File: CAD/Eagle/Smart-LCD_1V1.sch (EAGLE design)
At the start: 49 parts, among them Q121 MMBT2222AL, U101 MEGA8-P, U221 MCP4018T-104E/LT, U401 TS4871ID, X131 LDR, X141 Switches, X151 LEDs, X201 LCD_23WAY__UC1608, X231 LED_A, X232 LED_K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

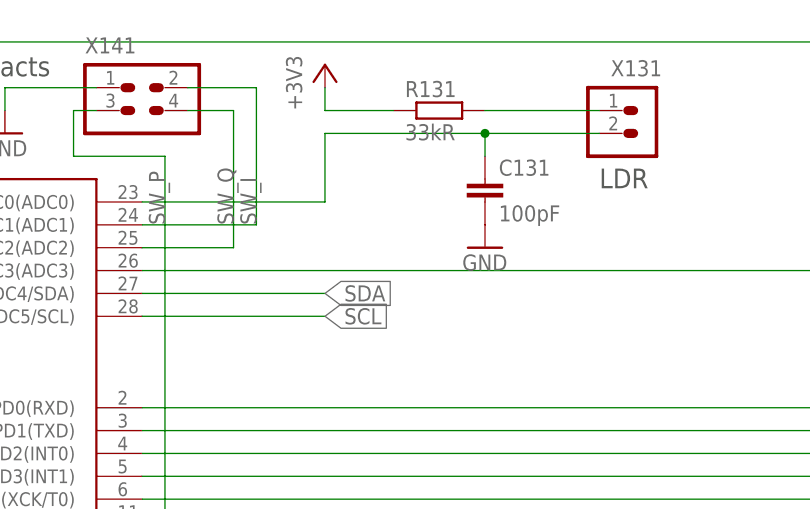
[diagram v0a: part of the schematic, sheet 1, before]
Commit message: CAD - new version V1.1 - missing resistor for LDR added, missing header pin number 1 marking added
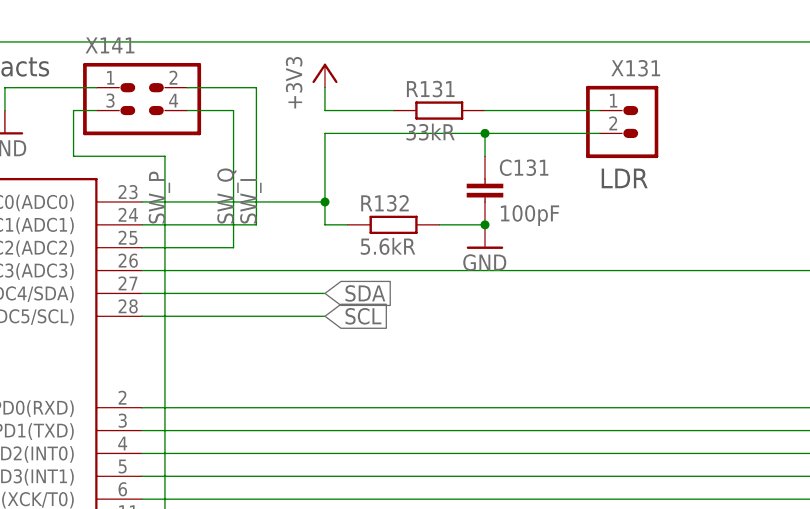
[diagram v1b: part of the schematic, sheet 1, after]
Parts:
- added R132: 5.6kR, rcl:R-EU_R0805
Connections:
- net GND: now also R132.2
- net LDR: now also R132.1
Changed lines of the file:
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@@
 <part name="C455" library="rcl" deviceset="C-EU" device="C0805" value="470nF"/>
 <part name="C452" library="rcl" deviceset="C-EU" device="C0805" value="470pF"/>
+<part name="R132" library="rcl" deviceset="R-EU_" device="R0805" value="5.6kR"/>
 </parts>
 <sheets>
@@
 <instance part="GND111" gate="1" x="154.94" y="53.34"/>
 <instance part="X141" gate="G$1" x="134.62" y="152.4"/>
+<instance part="R132" gate="G$1" x="162.56" y="137.16"/>
 </instances>
 <busses>
@@
 <pinref part="C131" gate="G$1" pin="2"/>
 <pinref part="GND131" gate="1" pin="GND"/>
+<pinref part="R132" gate="G$1" pin="2"/>
+<wire x1="172.72" y1="137.16" x2="167.64" y2="137.16" width="0.1524" layer="91"/>
+<junction x="172.72" y="137.16"/>
 </segment>
 <segment>
@@
 <pinref part="X131" gate="A" pin="2"/>
 <pinref part="U101" gate="G$1" pin="PC0(ADC0)"/>
-</segment>
-</net>
+<wire x1="154.94" y1="139.7" x2="154.94" y2="137.16" width="0.1524" layer="91"/>
+<pinref part="R132" gate="G$1" pin="1"/>
+<wire x1="154.94" y1="137.16" x2="157.48" y2="137.16" width="0.1524" layer="91"/>
+<junction x="154.94" y="139.7"/>
+</segment>
+</net>

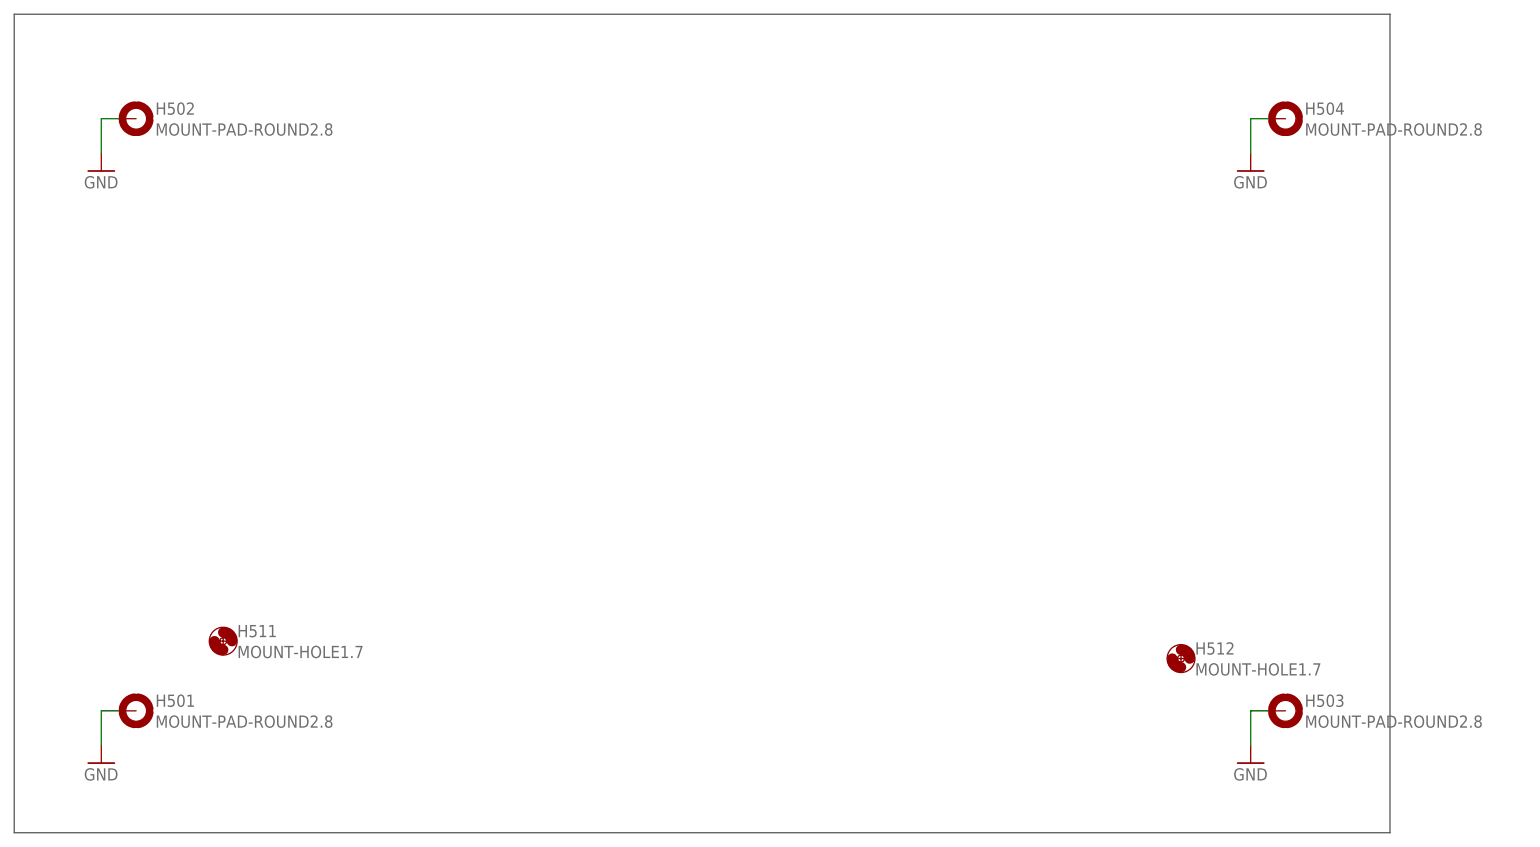
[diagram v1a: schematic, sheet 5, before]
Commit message: CAD - four fiducials added
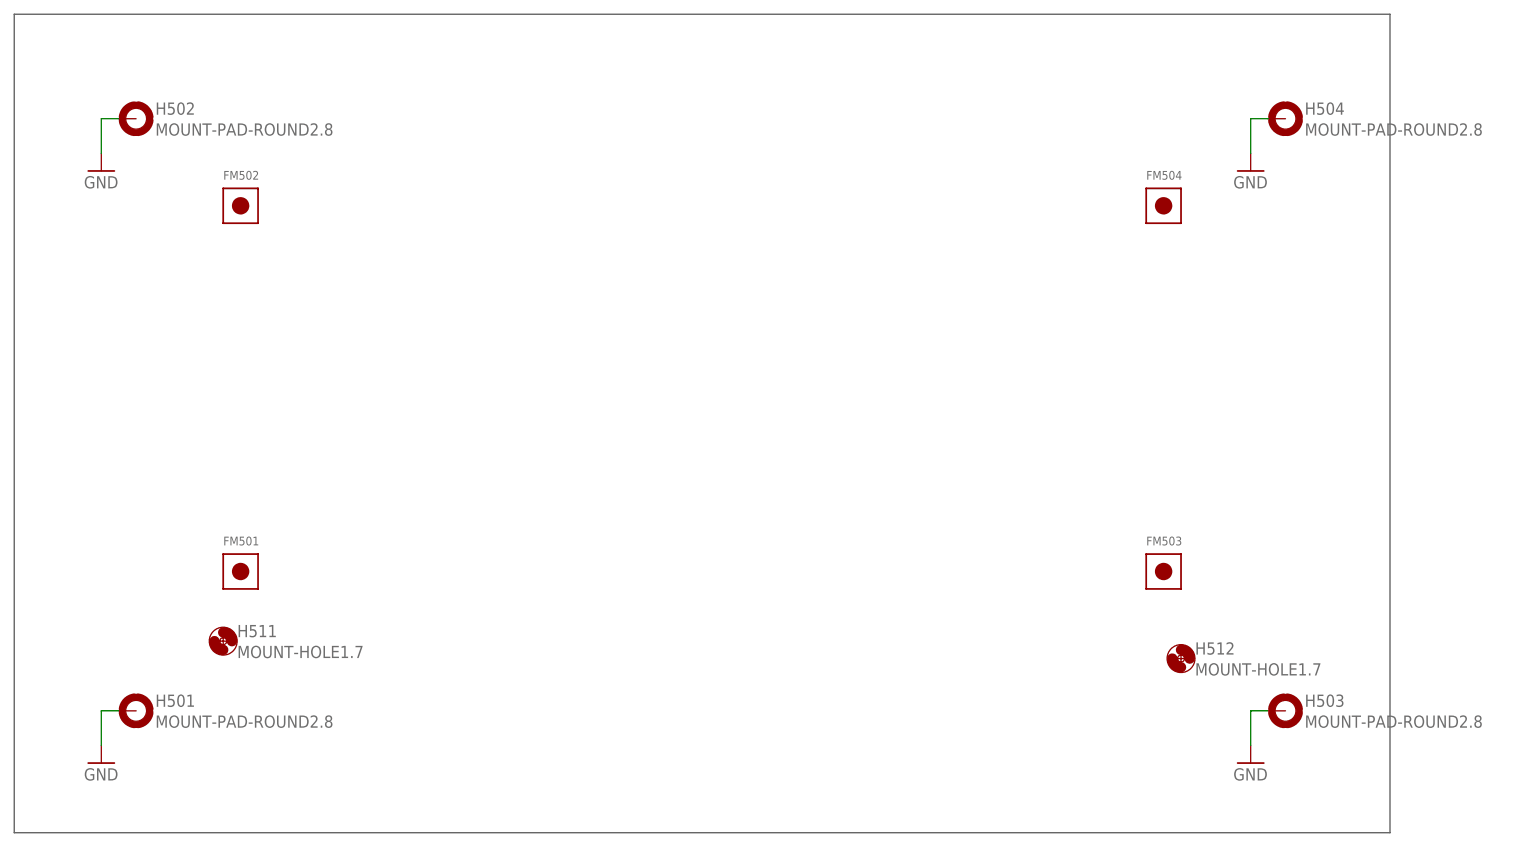
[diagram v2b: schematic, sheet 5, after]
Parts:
- added FM501, FM502, FM503, FM504: FIDUCIAL_MARK_1MM, df4iah_fiducial:FIDUCIAL_MARK_1MM
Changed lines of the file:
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@@
 <part name="C452" library="rcl" deviceset="C-EU" device="C0805" value="470pF"/>
 <part name="R132" library="rcl" deviceset="R-EU_" device="R0805" value="5.6kR"/>
+<part name="FM502" library="df4iah_fiducial" deviceset="FIDUCIAL_MARK_1MM" device=""/>
+<part name="FM501" library="df4iah_fiducial" deviceset="FIDUCIAL_MARK_1MM" device=""/>
+<part name="FM503" library="df4iah_fiducial" deviceset="FIDUCIAL_MARK_1MM" device=""/>
+<part name="FM504" library="df4iah_fiducial" deviceset="FIDUCIAL_MARK_1MM" device=""/>
 </parts>
 <sheets>
@@
 <instance part="H511" gate="G$1" x="55.88" y="68.58"/>
 <instance part="H512" gate="G$1" x="195.58" y="66.04"/>
+<instance part="FM502" gate="G$1" x="58.42" y="132.08"/>
+<instance part="FM501" gate="G$1" x="58.42" y="78.74"/>
+<instance part="FM503" gate="G$1" x="193.04" y="78.74"/>
+<instance part="FM504" gate="G$1" x="193.04" y="132.08"/>
 </instances>
 <busses>

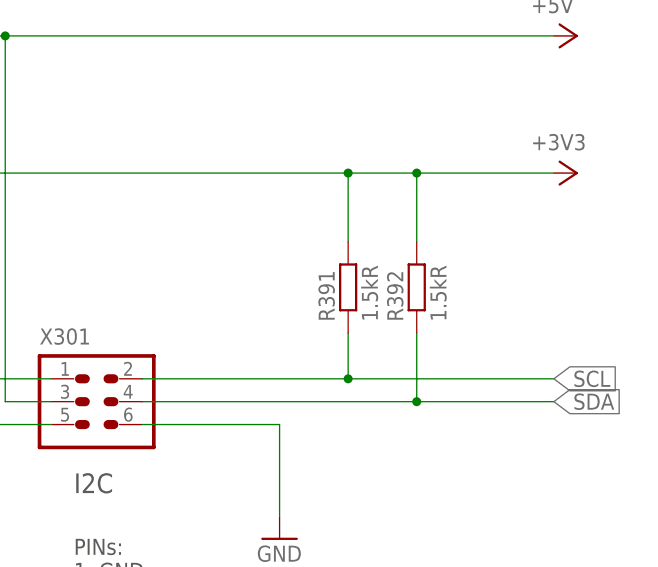
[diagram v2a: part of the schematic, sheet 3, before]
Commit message: HW_V1.1 - LCD backlight basis resistor chnaged to 4.7k ohms
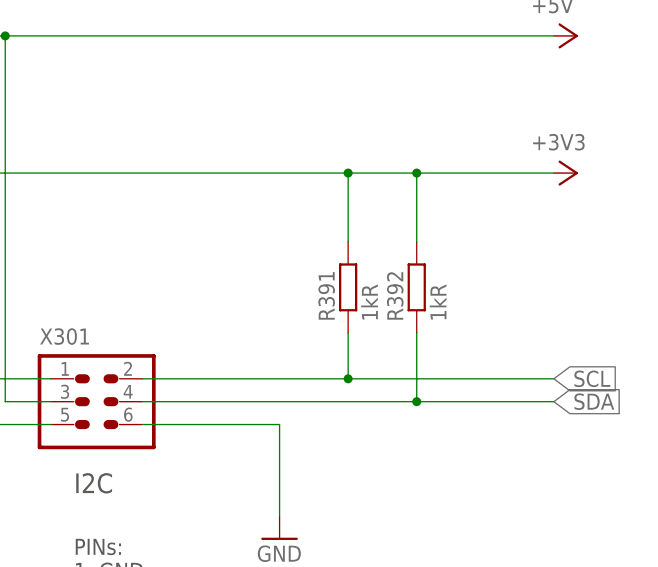
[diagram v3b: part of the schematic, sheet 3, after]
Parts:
- R121: value 18kR -> 4.7kR
- R391, R392: value 1.5kR -> 1kR; device rcl:R-EU_R0603 -> rcl:R-EU_R0805
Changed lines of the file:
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@@
 <part name="+3V3_301" library="df4iah_supply" deviceset="+3V3" device=""/>
 <part name="+5V0_301" library="df4iah_supply" deviceset="+5V" device=""/>
-<part name="R391" library="rcl" deviceset="R-EU_" device="R0603" value="1.5kR"/>
-<part name="R392" library="rcl" deviceset="R-EU_" device="R0603" value="1.5kR"/>
+<part name="R391" library="rcl" deviceset="R-EU_" device="R0805" value="1kR"/>
+<part name="R392" library="rcl" deviceset="R-EU_" device="R0805" value="1kR"/>
 <part name="FRAME4" library="df4iah_frame" deviceset="A4L-LOC" device="" value="Holes"/>
 <part name="X201" library="df4iah_connector" deviceset="LCD_23WAY__UC1608" device=""/>
@@
 <part name="C103" library="rcl" deviceset="C-EU" device="C0805" value="100pF"/>
 <part name="R101" library="rcl" deviceset="R-EU_" device="R0805" value="12kR"/>
-<part name="R121" library="rcl" deviceset="R-EU_" device="R0805" value="18kR"/>
+<part name="R121" library="rcl" deviceset="R-EU_" device="R0805" value="4.7kR"/>
 <part name="Q121" library="df4iah_bipoltransistor" deviceset="MMBT2222" device="" technology="AL"/>
 <part name="GND221" library="df4iah_supply" deviceset="GND" device=""/>

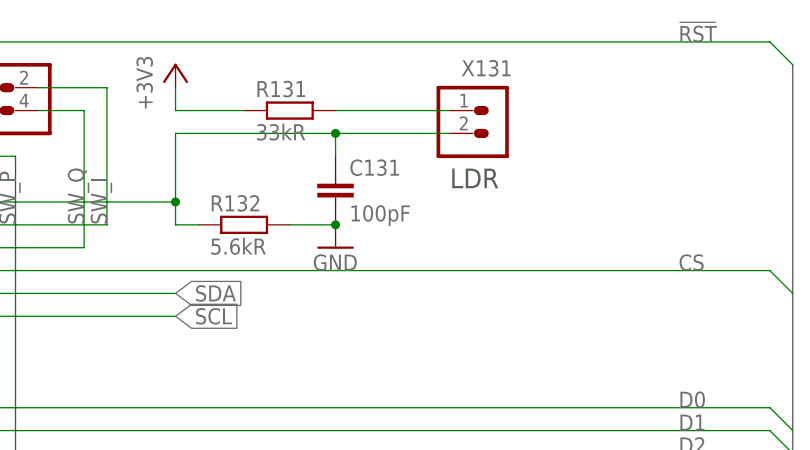
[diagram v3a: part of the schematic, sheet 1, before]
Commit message: HW_V1.1 - photo diode - resistor change from 100k to 1MR
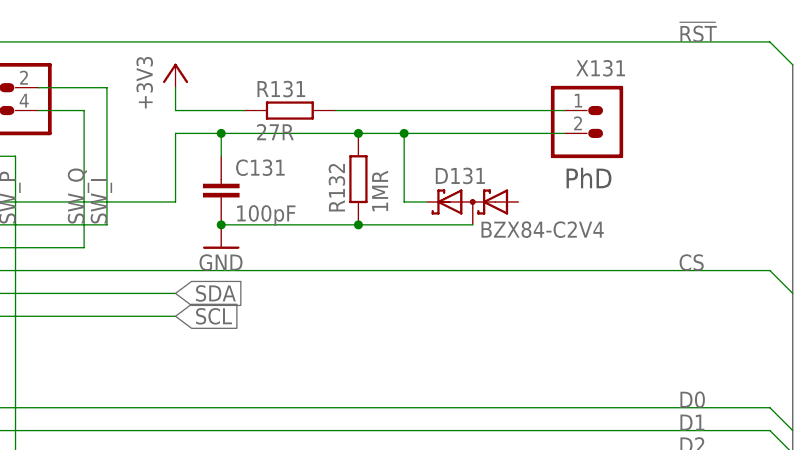
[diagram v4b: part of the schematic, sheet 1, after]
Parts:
- added D131: BZX84-C2V4, df4iah_diode:BAS70-04
- R131: value 33kR -> 27R
- R132: value 5.6kR -> 1MR
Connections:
- net GND: now also D131.C1A2, R132.1; no longer R132.2
- net LDR: now also D131.C2, R132.2; no longer R132.1
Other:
- note added: "PhD"
- note removed: "LDR"
- moved on the sheet: C131, R132, X131
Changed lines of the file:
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@@
 <part name="X131" library="df4iah_connector" deviceset="HEADER-1X2" device="" value="LDR"/>
 <part name="+3V3_131" library="df4iah_supply" deviceset="+3V3" device=""/>
-<part name="R131" library="rcl" deviceset="R-EU_" device="R0805" value="33kR"/>
+<part name="R131" library="rcl" deviceset="R-EU_" device="R0805" value="27R"/>
 <part name="C131" library="rcl" deviceset="C-EU" device="C0805" value="100pF"/>
 <part name="GND131" library="df4iah_supply" deviceset="GND" device=""/>
@@
 <part name="C455" library="rcl" deviceset="C-EU" device="C0805" value="470nF"/>
 <part name="C452" library="rcl" deviceset="C-EU" device="C0805" value="470pF"/>
-<part name="R132" library="rcl" deviceset="R-EU_" device="R0805" value="5.6kR"/>
+<part name="R132" library="rcl" deviceset="R-EU_" device="R0805" value="1MR"/>
 <part name="FM502" library="df4iah_fiducial" deviceset="FIDUCIAL_MARK_1MM" device=""/>
 <part name="FM501" library="df4iah_fiducial" deviceset="FIDUCIAL_MARK_1MM" device=""/>
 <part name="FM503" library="df4iah_fiducial" deviceset="FIDUCIAL_MARK_1MM" device=""/>
 <part name="FM504" library="df4iah_fiducial" deviceset="FIDUCIAL_MARK_1MM" device=""/>
+<part name="D131" library="df4iah_diode" deviceset="BAS70-04" device="" value="BZX84-C2V4"/>
 </parts>
 <sheets>
@@
 <description>MPU</description>
 <plain>
-<text x="185.42" y="141.224" size="2.1844" layer="97" ratio="12">LDR</text>
+<text x="198.12" y="141.224" size="2.1844" layer="97" ratio="12">PhD</text>
 <text x="112.522" y="153.67" size="2.1844" layer="97" ratio="12">Contacts</text>
 <text x="29.464" y="122.936" size="2.1844" layer="97" ratio="12">LEDs</text>
@@
 <instance part="Q121" gate="G$1" x="182.88" y="86.36"/>
 <instance part="GND121" gate="1" x="185.42" y="78.74"/>
-<instance part="X131" gate="A" x="187.96" y="149.86"/>
+<instance part="X131" gate="A" x="200.66" y="149.86"/>
 <instance part="+3V3_131" gate="G$1" x="154.94" y="154.94"/>
 <instance part="R131" gate="G$1" x="167.64" y="149.86"/>
-<instance part="C131" gate="G$1" x="172.72" y="142.24"/>
-<instance part="GND131" gate="1" x="172.72" y="134.62"/>
+<instance part="C131" gate="G$1" x="160.02" y="142.24"/>
+<instance part="GND131" gate="1" x="160.02" y="134.62"/>
 <instance part="GND141" gate="1" x="119.38" y="147.32"/>
 <instance part="X151" gate="G$1" x="33.02" y="132.08"/>
@@
 <instance part="GND111" gate="1" x="154.94" y="53.34"/>
 <instance part="X141" gate="G$1" x="134.62" y="152.4"/>
-<instance part="R132" gate="G$1" x="162.56" y="137.16"/>
+<instance part="R132" gate="G$1" x="175.26" y="142.24" rot="R90"/>
+<instance part="D131" gate="G$1" x="187.96" y="139.7" smashed="yes" rot="R180">
+<attribute name="NAME" x="183.642" y="141.7066" size="1.778" layer="95"/>
+<attribute name="VALUE" x="188.722" y="135.7376" size="1.778" layer="96"/>
+</instance>
 </instances>
 <busses>
@@
 <pinref part="C131" gate="G$1" pin="2"/>
 <pinref part="GND131" gate="1" pin="GND"/>
-<pinref part="R132" gate="G$1" pin="2"/>
-<wire x1="172.72" y1="137.16" x2="167.64" y2="137.16" width="0.1524" layer="91"/>
-<junction x="172.72" y="137.16"/>
+<junction x="160.02" y="137.16"/>
+<pinref part="R132" gate="G$1" pin="1"/>
+<wire x1="160.02" y1="137.16" x2="175.26" y2="137.16" width="0.1524" layer="91"/>
+<junction x="175.26" y="137.16"/>
+<pinref part="D131" gate="G$1" pin="C1A2"/>
+<wire x1="175.26" y1="137.16" x2="187.96" y2="137.16" width="0.1524" layer="91"/>
 </segment>
 <segment>
@@
 <wire x1="134.62" y1="139.7" x2="154.94" y2="139.7" width="0.1524" layer="91"/>
 <wire x1="154.94" y1="139.7" x2="154.94" y2="147.32" width="0.1524" layer="91"/>
-<wire x1="154.94" y1="147.32" x2="172.72" y2="147.32" width="0.1524" layer="91"/>
+<wire x1="154.94" y1="147.32" x2="160.02" y2="147.32" width="0.1524" layer="91"/>
 <pinref part="C131" gate="G$1" pin="1"/>
-<wire x1="172.72" y1="147.32" x2="185.42" y2="147.32" width="0.1524" layer="91"/>
-<wire x1="172.72" y1="147.32" x2="172.72" y2="144.78" width="0.1524" layer="91"/>
-<junction x="172.72" y="147.32"/>
+<wire x1="160.02" y1="147.32" x2="160.02" y2="144.78" width="0.1524" layer="91"/>
+<junction x="160.02" y="147.32"/>
+<pinref part="U101" gate="G$1" pin="PC0(ADC0)"/>
+<pinref part="R132" gate="G$1" pin="2"/>
+<wire x1="160.02" y1="147.32" x2="175.26" y2="147.32" width="0.1524" layer="91"/>
+<junction x="175.26" y="147.32"/>
 <pinref part="X131" gate="A" pin="2"/>
-<pinref part="U101" gate="G$1" pin="PC0(ADC0)"/>
-<wire x1="154.94" y1="139.7" x2="154.94" y2="137.16" width="0.1524" layer="91"/>
-<pinref part="R132" gate="G$1" pin="1"/>
-<wire x1="154.94" y1="137.16" x2="157.48" y2="137.16" width="0.1524" layer="91"/>
-<junction x="154.94" y="139.7"/>
+<wire x1="175.26" y1="147.32" x2="180.34" y2="147.32" width="0.1524" layer="91"/>
+<wire x1="180.34" y1="147.32" x2="198.12" y2="147.32" width="0.1524" layer="91"/>
+<wire x1="180.34" y1="147.32" x2="180.34" y2="139.7" width="0.1524" layer="91"/>
+<pinref part="D131" gate="G$1" pin="C2"/>
+<wire x1="180.34" y1="139.7" x2="182.88" y2="139.7" width="0.1524" layer="91"/>
+<junction x="180.34" y="147.32"/>
 </segment>
 </net>
@@
 <pinref part="X131" gate="A" pin="1"/>
 <pinref part="R131" gate="G$1" pin="2"/>
-<wire x1="185.42" y1="149.86" x2="172.72" y2="149.86" width="0.1524" layer="91"/>
-</segment>
-</net>
+<wire x1="198.12" y1="149.86" x2="172.72" y2="149.86" width="0.1524" layer="91"/>
+</segment>
+</net>
